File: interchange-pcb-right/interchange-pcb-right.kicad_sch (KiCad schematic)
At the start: 79 parts, among them J1 Conn_01x04, J2 Conn_01x04, J3 TRRS_L, J4 TRRS_R, J5 SSD1306, SW1 RotaryEncoder, U1 Seeeduino Xiao rp2040, U2 PCA9555PW, U3 PCA9555PW, U4 ADS1110, U5 SN74AHCT125PWR, U6 TCA4307DGKR

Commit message: feat(right): add LCSC part numbers to schematics
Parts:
- BZ1: LCSC (none) -> C94599
- C31, C32, C33, C34, C35, C36: LCSC (none) -> C14663
- LED31: LCSC (none) -> C5149201
- MX1, MX10, MX11, MX12, MX13, MX14, MX15, MX16, MX17, MX18, MX19, MX2, MX20, MX21, MX22, MX23, MX24, MX25, MX26, MX27, MX28, MX29, MX3, MX30, MX4, MX5, MX6, MX7, MX8, MX9: LCSC (none) -> C41430893
- R1, R10, R2, R7, R8, R9: LCSC (none) -> C4190
- R3, R4, R6: LCSC (none) -> C25804
- R5: LCSC (none) -> C4260
- U2, U3: LCSC (none) -> C128392
- U4: LCSC (none) -> C16598
- U5: LCSC (none) -> C36365
- U6: LCSC (none) -> C880333

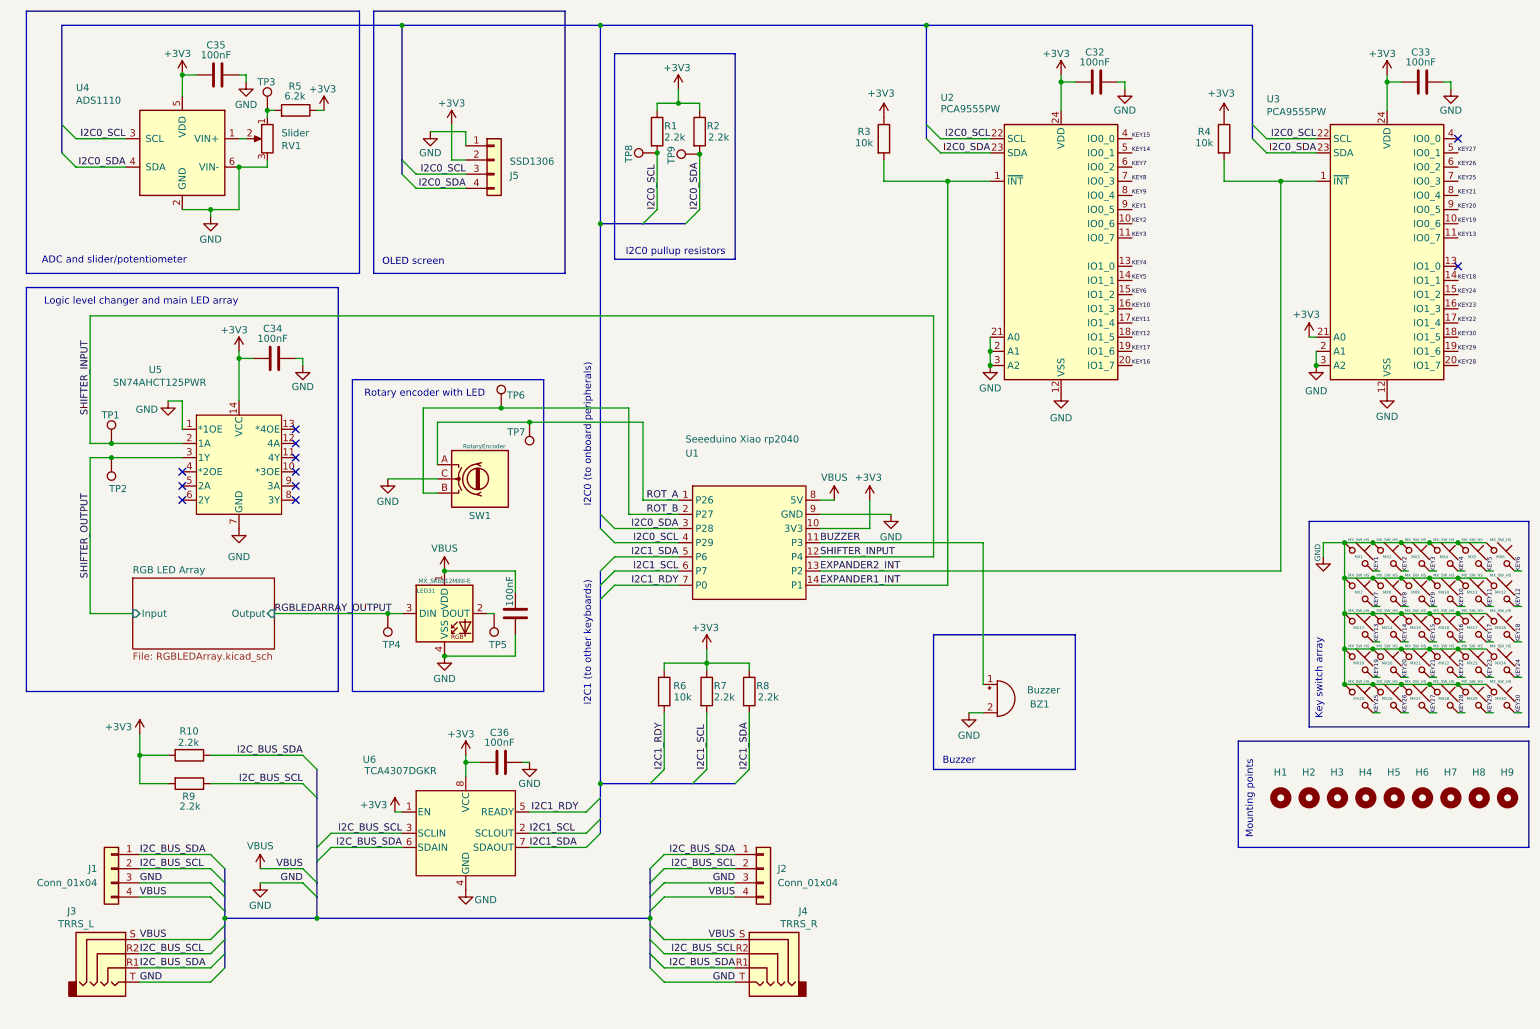
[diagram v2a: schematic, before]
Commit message: wip: add reverse polarity protection and fix buzzer
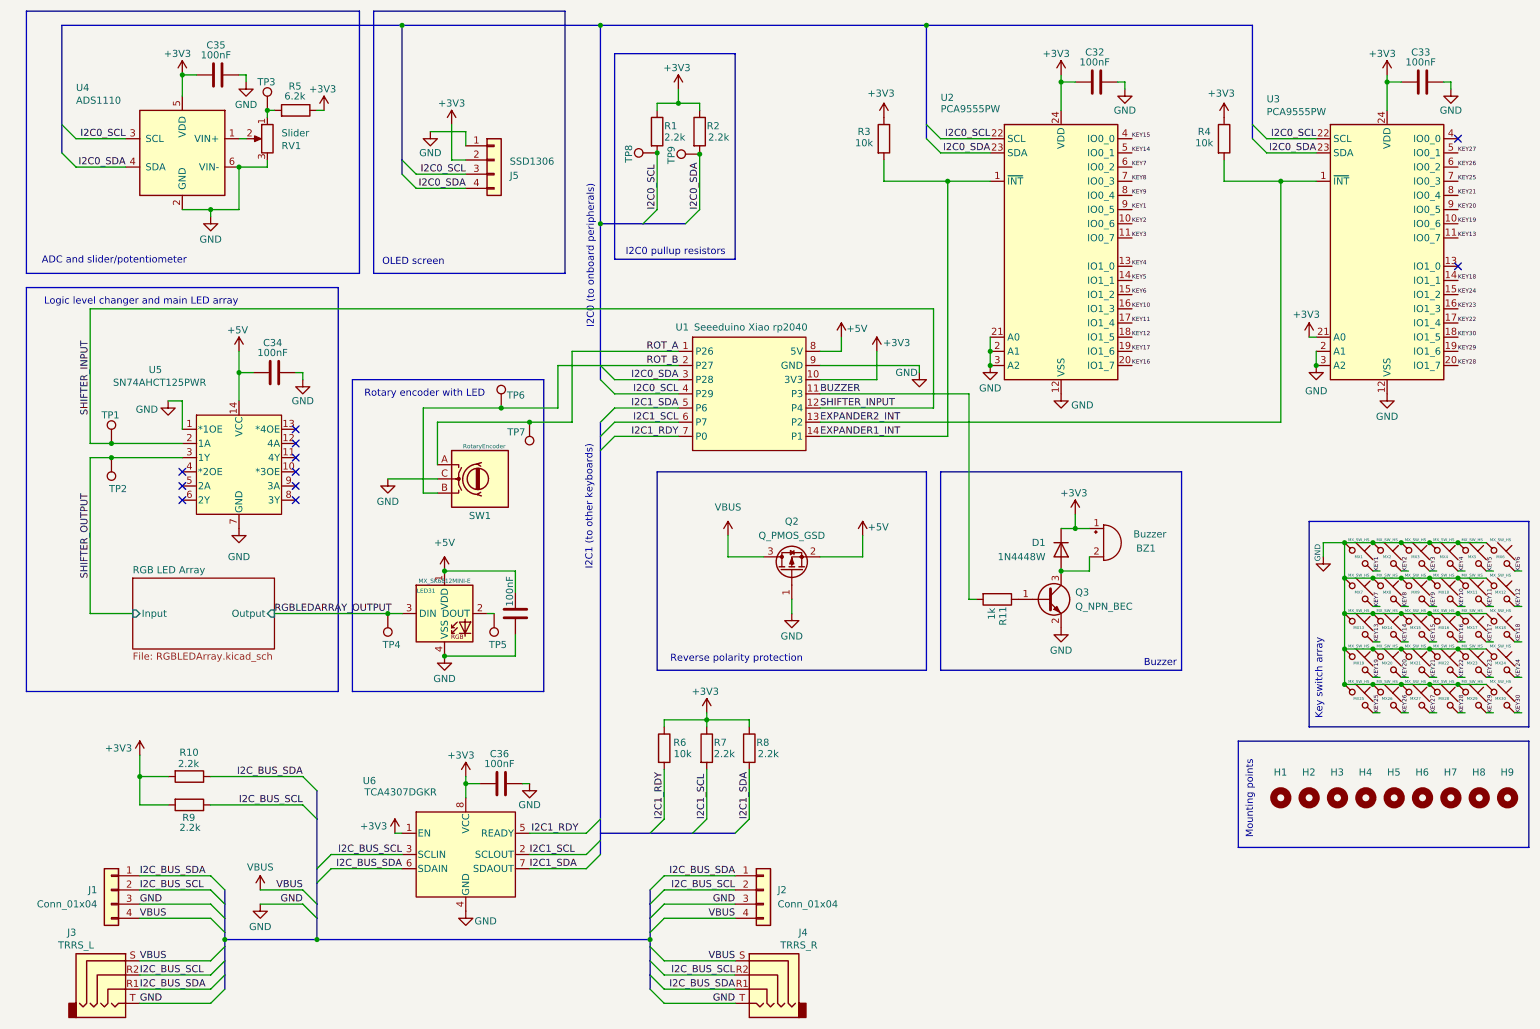
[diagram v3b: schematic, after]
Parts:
- added D1: 1N4448W, Diode_SMD:D_SOD-123, symbol Diode:1N4448W
- added Q2: Q_PMOS_GSD, Package_TO_SOT_SMD:SOT-23_Handsoldering, symbol Transistor_FET:Q_PMOS_GSD
- added Q3: Q_NPN_BEC, Package_TO_SOT_SMD:SOT-23_Handsoldering, symbol Transistor_BJT:Q_NPN_BEC
- added R11: 1k, Resistor_SMD:R_0603_1608Metric_Pad0.98x0.95mm_HandSolder, symbol Device:R
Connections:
- net +3V3: now also BZ1.1 (+), D1.1 (K); no longer C34.2, U5.14 (VCC)
- net BUZZER: now also R11.2; no longer BZ1.1 (+)
- net GND: now also Q2.1 (G), Q3.2 (E); no longer BZ1.2 (-)
- net VBUS: now also Q2.3 (D); no longer C31.2, LED31.1 (VDD), U1.8 (5V)
- new net: BZ1.2 (-), D1.2 (A), Q3.3 (C)
- new net: Q3.1 (B), R11.1
- new net +5V: C31.2, C34.2, LED31.1 (VDD), Q2.2 (S), U1.8 (5V), U5.14 (VCC)
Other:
- note added: "Reverse polarity protection"
- moved on the sheet: C34, C36, J1, J2, J3, J4, R10, R6, R7, R8, R9, U6

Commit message: feat(right): add more mounting holes
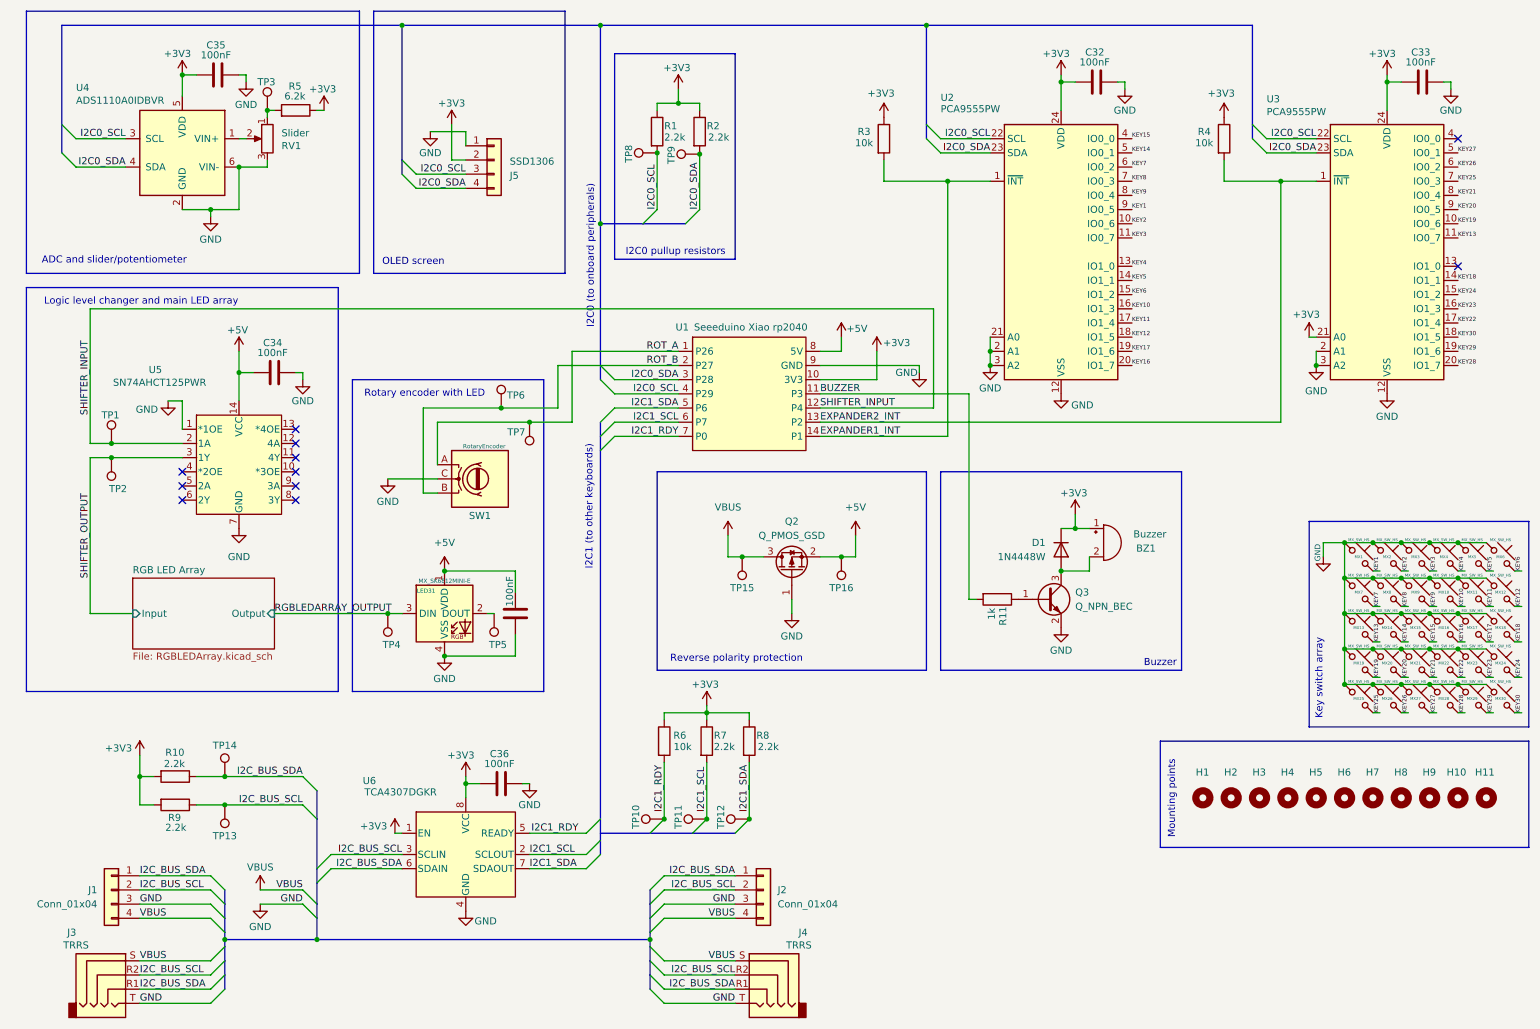
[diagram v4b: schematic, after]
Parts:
- added H10, H11: MountingHole_Pad, MountingHole:MountingHole_3.2mm_M3, symbol Mechanical:MountingHole
- added TP10, TP11, TP12, TP13, TP14, TP15, TP16: TestPoint, TestPoint:TestPoint_Pad_D1.5mm, symbol Connector:TestPoint
- J3: value TRRS_L -> TRRS; LCSC (none) -> C95562
- J4: value TRRS_R -> TRRS; LCSC (none) -> C95562
- J5: LCSC (none) -> C5248081
- R11: LCSC (none) -> C2907113
- R3, R4, R6: LCSC C25804 -> C2930027
- R5: LCSC C4260 -> C2907186
- RV1: LCSC (none) -> C470640
- SW1: LCSC (none) -> C351235
- U4: value ADS1110 -> ADS1110A0IDBVR
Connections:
- net +5V: now also TP16.1
- net I2C1_RDY: now also TP10.1
- net I2C1_SCL: now also TP11.1
- net I2C1_SDA: now also TP12.1
- net I2C_BUS_SCL: now also TP13.1
- net I2C_BUS_SDA: now also TP14.1
- net VBUS: now also TP15.1
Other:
- moved on the sheet: H1, H2, H3, H4, H5, H6, H7, H8, H9, R10, R6, R7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

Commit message: wip
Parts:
- removed C36: 100nF, Capacitor_SMD:C_0603_1608Metric_Pad1.08x0.95mm_HandSolder, symbol Device:C
- removed R10, R8, R9: 2.2k, Resistor_SMD:R_0603_1608Metric_Pad0.98x0.95mm_HandSolder, symbol Device:R
- removed TP12, TP13, TP14: TestPoint, TestPoint:TestPoint_Pad_D1.5mm, symbol Connector:TestPoint
- removed U6: TCA4307DGKR, CustomFootprints:SOIC8_DGK_TEX, symbol CustomSymbols:TCA4307DGKR
- R7: value 2.2k -> 10k; LCSC C4190 -> C2930027
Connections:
- net I2C1_SDA is gone; now on net EBD: U1.5 (P6)
- net I2C_BUS_SCL is gone; now on net EBC: J1.2 (Pin_2), J2.2 (Pin_2), J3.R2, J4.R2
- net I2C_BUS_SDA is gone; now on net EBD: J1.1 (Pin_1), J2.1 (Pin_1), J3.R1, J4.R1
- net I2C1_RDY renamed EBD
- net EBD: no longer U1.7 (P0)
- net I2C1_SCL renamed EBC
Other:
- note added: "EDBUS (link with other keyboards)"
- note added: "TODO!!! HOW DOES POWER FLOW FROM PICO TO OTHER PICOS AFFECT THIS?"
- note removed: "I2C1 (to other keyboards)"
- moved on the sheet: R6, TP10, TP11
